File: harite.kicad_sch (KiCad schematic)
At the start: 10 parts

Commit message: Layout switches
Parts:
- removed S6: SKRHADE010, SKRHADE010, symbol SKRHADE010:SKRHADE010
- added D10, D11, D12, D13, D14, D15, D16, D17, D18, D19, D20, D21, D22, D23, D24, D25, D5, D6, D7, D8, D9: D, footprints:D_SOD123, symbol Device:D
- added U1: rp2040-zero, footprints:rp2040-zero-tht, symbol mcu:rp2040-zero
- D1, D2, D3, D4: footprint (none) -> footprints:D_SOD123
- S1, S2, S3, S4, S5: footprint SKRHADE010 -> footprints:SKRHADE010
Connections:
- net at S1.2 (CENTER): now also D5.2 (A)
- net at S1.3 (C): now also D2.2 (A)
- net at S1.4 (B): now also D4.2 (A)
- net Col 1: now reaches S1.5 (COMMON)
- net Col 1: now also U1.10 (9)
- net at S1.6 (D): now also D3.2 (A)
- net at S3.1 (A): now also D11.2 (A)
- net at S3.2 (CENTER): now also D12.2 (A)
- net at S3.3 (C): now also D13.2 (A)
- net at S3.4 (B): now also D14.2 (A)
- net Col 3: now reaches S3.5 (COMMON)
- net Col 3: now also U1.12 (11)
- net at S3.6 (D): now also D15.2 (A)
- net Row 1: now reaches D1.1 (K)
- net Row 1: now also D11.1 (K), D16.1 (K), D21.1 (K), D6.1 (K), U1.15 (14)
- net at S2.1 (A): now also D6.2 (A)
- net at S2.2 (CENTER): now also D7.2 (A)
- net at S2.3 (C): now also D8.2 (A)
- net at S2.4 (B): now also D9.2 (A)
- net Col 2: now reaches S2.5 (COMMON)
- net Col 2: now also U1.11 (10)
- net at S2.6 (D): now also D10.2 (A)
- net at S4.1 (A): now also D16.2 (A)
- net at S4.2 (CENTER): now also D17.2 (A)
- net at S4.3 (C): now also D18.2 (A)
- net at S4.4 (B): now also D19.2 (A)
- net Col 4: now reaches S4.5 (COMMON)
- net Col 4: now also U1.13 (12)
- net at S4.6 (D): now also D20.2 (A)
- net Row 5: now reaches D3.1 (K)
- net Row 5: now also D10.1 (K), D15.1 (K), D20.1 (K), D25.1 (K), U1.19 (28)
- net Row 4: now reaches D4.1 (K)
- net Row 4: now also D14.1 (K), D19.1 (K), D24.1 (K), D9.1 (K), U1.18 (27)
- net Row 2: now reaches D2.1 (K)
- net Row 2: now also D13.1 (K), D18.1 (K), D23.1 (K), D8.1 (K), U1.16 (15)
- net at S5.1 (A): now also D21.2 (A)
- net at S5.2 (CENTER): now also D22.2 (A)
- net at S5.3 (C): now also D23.2 (A)
- net at S5.4 (B): now also D24.2 (A)
- net Col 5: now reaches S5.5 (COMMON)
- net Col 5: now also U1.14 (13)
- net at S5.6 (D): now also D25.2 (A)
- new net Row 3: D12.1 (K), D17.1 (K), D22.1 (K), D5.1 (K), D7.1 (K), U1.17 (26)
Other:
- moved on the sheet: S1

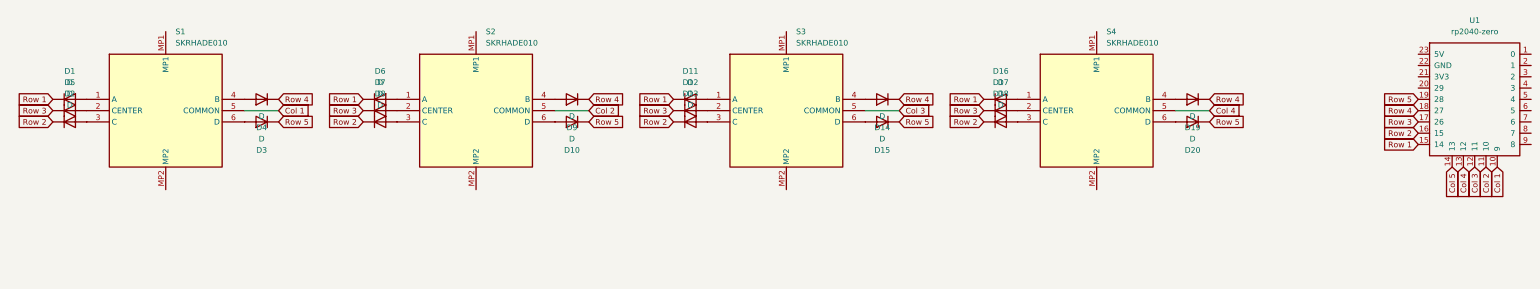
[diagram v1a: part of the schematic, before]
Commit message: Add scottokeebs
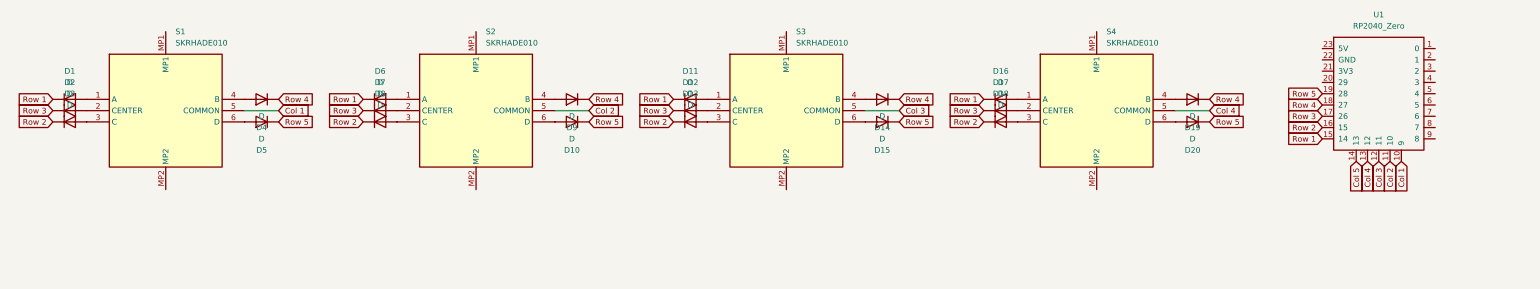
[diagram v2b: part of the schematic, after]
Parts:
- removed U1: rp2040-zero, footprints:rp2040-zero-tht, symbol mcu:rp2040-zero
- added U1: RP2040_Zero, ScottoKeebs_MCU:RP2040_Zero, symbol ScottoKeebs:MCU_RP2040_Zero
- D1, D10, D11, D12, D13, D14, D15, D16, D17, D18, D19, D20, D21, D22, D23, D24, D25, D4, D6, D7, D8, D9: footprint footprints:D_SOD123 -> ScottoKeebs_Components:Diode_SOD-123
- D2: renamed from D5; footprint footprints:D_SOD123 -> ScottoKeebs_Components:Diode_SOD-123
- D3: renamed from D2; footprint footprints:D_SOD123 -> ScottoKeebs_Components:Diode_SOD-123
- D5: renamed from D3; footprint footprints:D_SOD123 -> ScottoKeebs_Components:Diode_SOD-123
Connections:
- net Col 1: now also U1.10 (9)
- net Col 2: now also U1.11 (10)
- net Col 3: now also U1.12 (11)
- net Col 4: now also U1.13 (12)
- net Col 5: now also U1.14 (13)
- net Row 1: now also U1.15 (14)
- net Row 2: now also U1.16 (15)
- net Row 3: now also U1.17 (26)
- net Row 4: now also U1.18 (27)
- net Row 5: now also U1.19 (28)

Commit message: Add trrs
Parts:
- added U2: TRRS, ScottoKeebs_Components:TRRS_PJ-320A, symbol ScottoKeebs:Placeholder_TRRS
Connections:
- net Row 2: now also D12.1 (K), D17.1 (K), D2.1 (K), D22.1 (K), D7.1 (K); no longer D13.1 (K), D18.1 (K), D23.1 (K), D3.1 (K), D8.1 (K)
- net Row 3: now also D13.1 (K), D18.1 (K), D23.1 (K), D3.1 (K), D8.1 (K); no longer D12.1 (K), D17.1 (K), D2.1 (K), D22.1 (K), D7.1 (K)
- net GP0: now reaches U1.1 (0)
- net GP0: now also U2.4 (RING2)
- net GP1: now reaches U1.2 (1)
- net GP1: now also U2.3 (RING1)
- net 3V3: now reaches U1.21 (3V3)
- net GND: now reaches U1.22 (GND)
- net GND: now also U2.1 (SLEEVE)
- net 5V: now reaches U1.23 (5V)
- net 5V: now also U2.2 (TIP)

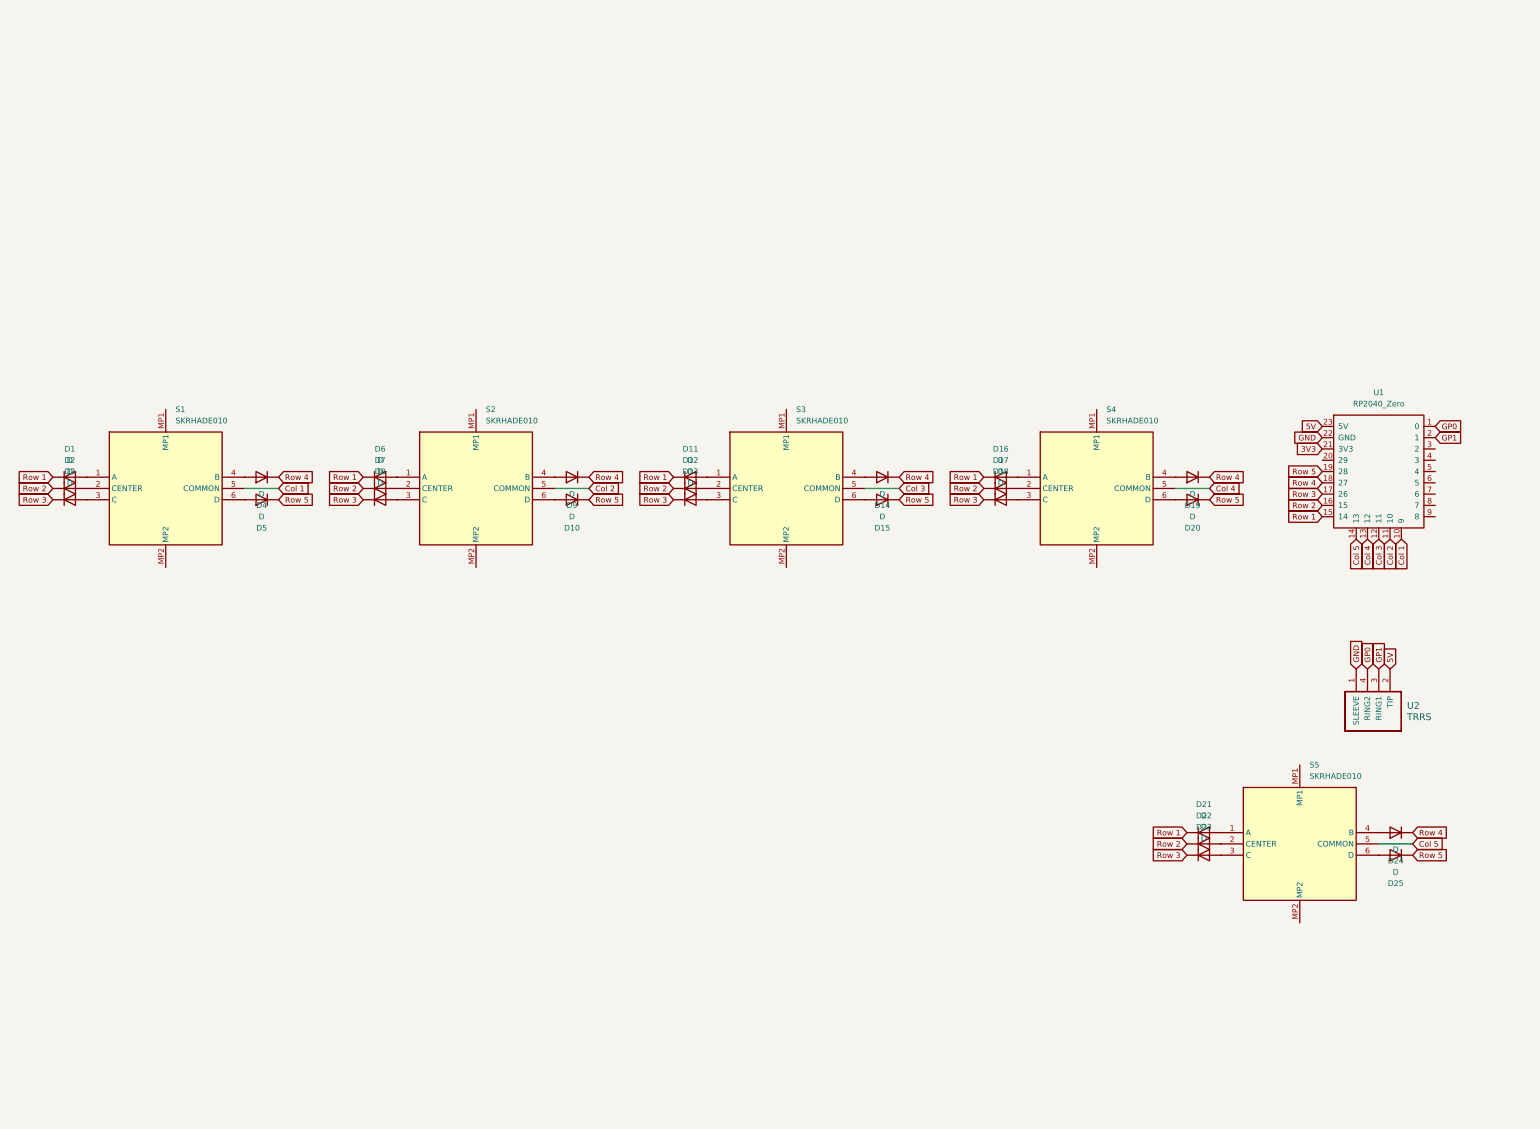
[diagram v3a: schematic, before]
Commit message: Add usbc and cirque
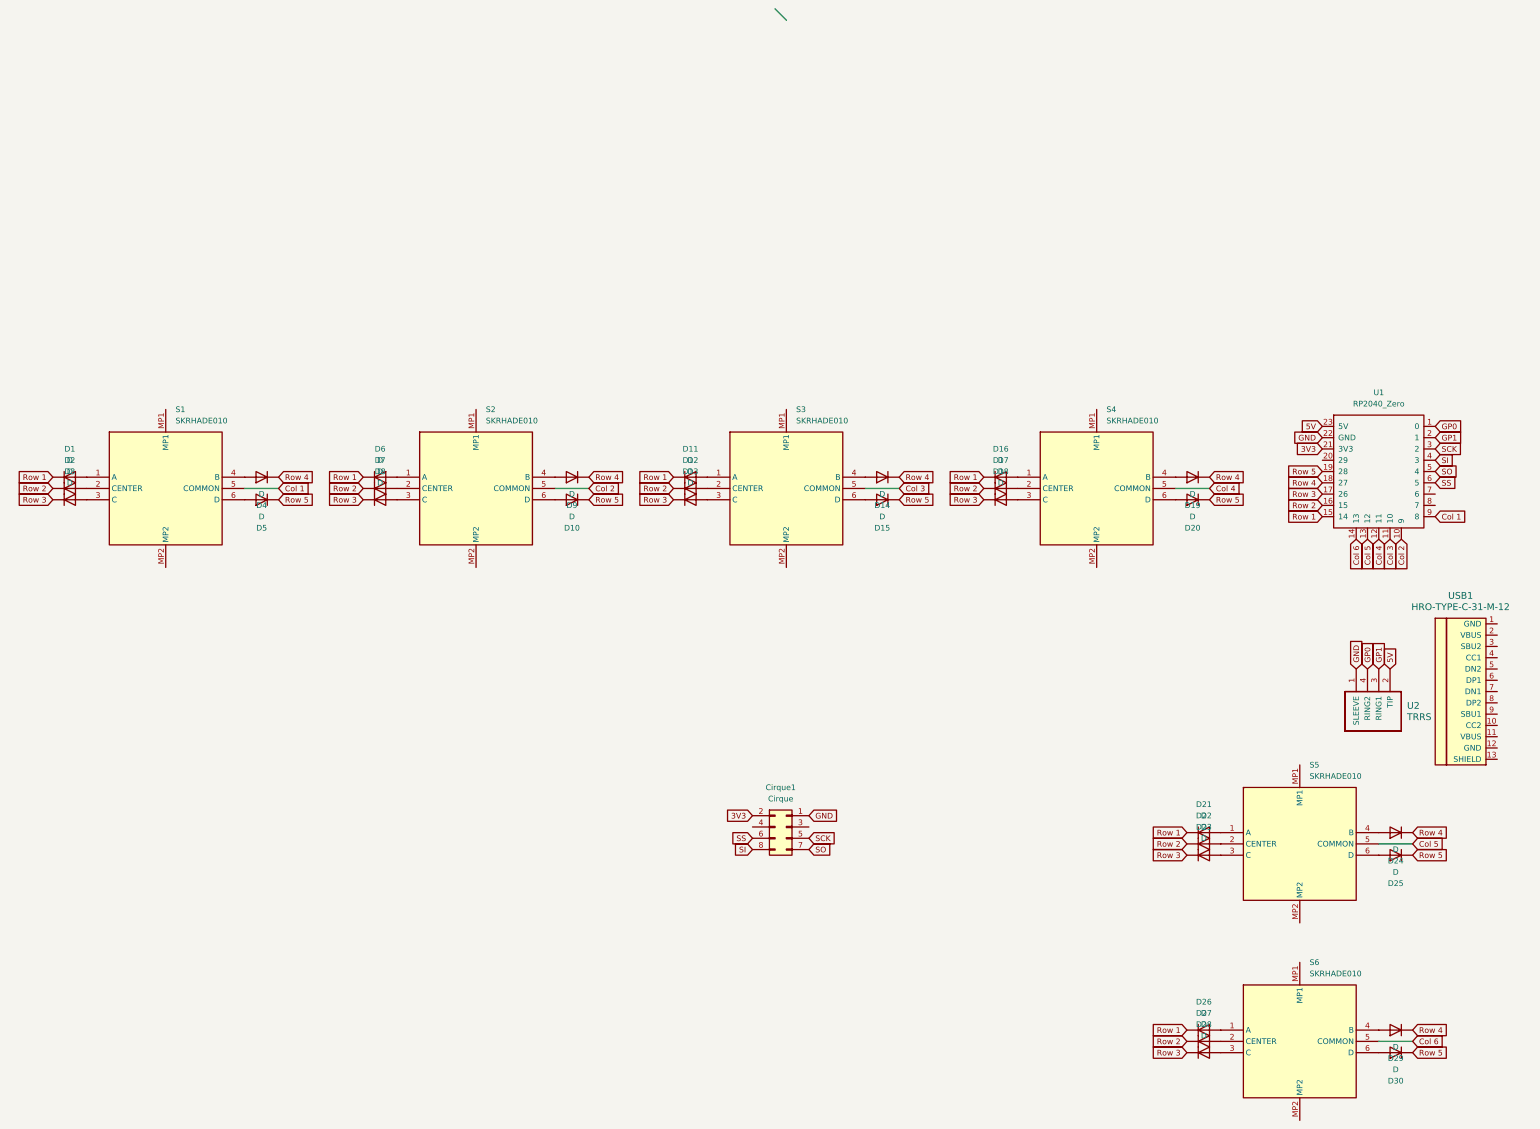
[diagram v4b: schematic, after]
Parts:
- added Cirque1: Cirque, footprints:CIRQUE-TM040040, symbol Connector_Generic:Conn_02x04_Top_Bottom
- added D26, D27, D28, D29, D30: D, ScottoKeebs_Components:Diode_SOD-123, symbol Device:D
- added S6: SKRHADE010, footprints:SKRHADE010, symbol SKRHADE010:SKRHADE010
- added USB1: HRO-TYPE-C-31-M-12, ScottoKeebs_Components:USB_C_HRO_TYPE-C-31-M-12, symbol USBType-C:HRO-TYPE-C-31-M-12
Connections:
- net 3V3: now also Cirque1.2 (Pin_2)
- net Col 1: now also U1.9 (8); no longer U1.10 (9)
- net Col 2: now also U1.10 (9); no longer U1.11 (10)
- net Col 3: now also U1.11 (10); no longer U1.12 (11)
- net Col 4: now also U1.12 (11); no longer U1.13 (12)
- net Col 5: now also U1.13 (12); no longer U1.14 (13)
- net GND: now also Cirque1.1 (Pin_1)
- net Row 1: now also D26.1 (K)
- net Row 2: now also D27.1 (K)
- net Row 3: now also D28.1 (K)
- net Row 4: now also D29.1 (K)
- net Row 5: now also D30.1 (K)
- net SCK: now reaches U1.3 (2)
- net SCK: now also Cirque1.5 (Pin_5)
- net SI: now reaches U1.4 (3)
- net SI: now also Cirque1.8 (Pin_8)
- net SO: now reaches U1.5 (4)
- net SO: now also Cirque1.7 (Pin_7)
- net SS: now reaches U1.6 (5)
- net SS: now also Cirque1.6 (Pin_6)
- new net: D27.2 (A), S6.2 (CENTER)
- new net: D26.2 (A), S6.1 (A)
- new net: D28.2 (A), S6.3 (C)
- new net: D29.2 (A), S6.4 (B)
- new net: D30.2 (A), S6.6 (D)
- new net Col 6: S6.5 (COMMON), U1.14 (13)

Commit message: update usbc
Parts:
- removed U2: TRRS, ScottoKeebs_Components:TRRS_PJ-320A, symbol ScottoKeebs:Placeholder_TRRS
- USB1: footprint ScottoKeebs_Components:USB_C_HRO_TYPE-C-31-M-12 -> footprints:HRO-TYPE-C-31-M-12
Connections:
- net 5V: now also USB1.2 (VBUS)
- net GND: now also USB1.1 (GND), USB1.12 (GND), USB1.13 (SHIELD)
- net GP0: now also USB1.5 (DN2), USB1.6 (DP1)
- net GP1: now also USB1.7 (DN1), USB1.8 (DP2)
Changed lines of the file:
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@@
 		)
 	)
-	(global_label "5V"
+	(global_label "GP0"
 		(shape input)
-		(at 321.31 99.06 90)
+		(at 345.44 101.6 0)
 		(fields_autoplaced yes)
 		(effects
@@
 		)
 		(property "Intersheetrefs" "${INTERSHEET_REFS}"
-			(at 321.31 93.7767 90)
+			(at 352.1747 101.6 0)
 			(effects
 				(font
@@
 		)
 	)
-	(global_label "GP1"
+	(global_label "Row 2"
+		(shape input)
+		(at 90.17 58.42 180)
+		(fields_autoplaced yes)
+		(effects
+			(font
+				(size 1.27 1.27)
+			)
+			(justify right)
+		)
+		(property "Intersheetrefs" "${INTERSHEET_REFS}"
+			(at 81.2582 58.42 0)
+			(effects
+				(font
+					(size 1.27 1.27)
+				)
+				(justify right)
+				(hide yes)
+			)
+		)
+	)
+	(global_label "SO"
 		(shape input)
-		(at 318.77 99.06 90)
+		(at 331.47 54.61 0)
 		(fields_autoplaced yes)
 		(effects
@@
 		)
 		(property "Intersheetrefs" "${INTERSHEET_REFS}"
-			(at 318.77 92.3253 90)
+			(at 336.9952 54.61 0)
 			(effects
 				(font
@@
 		)
 	)
-	(global_label "Row 2"
+	(global_label "Row 1"
 		(shape input)
-		(at 90.17 58.42 180)
+		(at 90.17 55.88 180)
 		(fields_autoplaced yes)
 		(effects
@@
 		)
 		(property "Intersheetrefs" "${INTERSHEET_REFS}"
-			(at 81.2582 58.42 0)
+			(at 81.2582 55.88 0)
 			(effects
 				(font
@@
 		)
 	)
-	(global_label "SO"
+	(global_label "GP1"
 		(shape input)
-		(at 331.47 54.61 0)
+		(at 345.44 104.14 0)
 		(fields_autoplaced yes)
 		(effects
@@
 		)
 		(property "Intersheetrefs" "${INTERSHEET_REFS}"
-			(at 336.9952 54.61 0)
+			(at 352.1747 104.14 0)
 			(effects
 				(font
@@
 		)
 	)
-	(global_label "Row 1"
+	(global_label "GND"
 		(shape input)
-		(at 90.17 55.88 180)
+		(at 345.44 88.9 0)
 		(fields_autoplaced yes)
 		(effects
@@
 				(size 1.27 1.27)
 			)
-			(justify right)
+			(justify left)
 		)
 		(property "Intersheetrefs" "${INTERSHEET_REFS}"
-			(at 81.2582 55.88 0)
+			(at 352.2957 88.9 0)
 			(effects
 				(font
 					(size 1.27 1.27)
 				)
-				(justify right)
+				(justify left)
 				(hide yes)
 			)
@@
 		)
 	)
+	(global_label "5V"
+		(shape input)
+		(at 345.44 91.44 0)
+		(fields_autoplaced yes)
+		(effects
+			(font
+				(size 1.27 1.27)
+			)
+			(justify left)
+		)
+		(property "Intersheetrefs" "${INTERSHEET_REFS}"
+			(at 350.7233 91.44 0)
+			(effects
+				(font
+					(size 1.27 1.27)
+				)
+				(justify left)
+				(hide yes)
+			)
+		)
+	)
+	(global_label "GND"
+		(shape input)
+		(at 345.44 116.84 0)
+		(fields_autoplaced yes)
+		(effects
+			(font
+				(size 1.27 1.27)
+			)
+			(justify left)
+		)
+		(property "Intersheetrefs" "${INTERSHEET_REFS}"
+			(at 352.2957 116.84 0)
+			(effects
+				(font
+					(size 1.27 1.27)
+				)
+				(justify left)
+				(hide yes)
+			)
+		)
+	)
 	(global_label "SCK"
 		(shape input)
@@
 		)
 	)
+	(global_label "GP0"
+		(shape input)
+		(at 345.44 99.06 0)
+		(fields_autoplaced yes)
+		(effects
+			(font
+				(size 1.27 1.27)
+			)
+			(justify left)
+		)
+		(property "Intersheetrefs" "${INTERSHEET_REFS}"
+			(at 352.1747 99.06 0)
+			(effects
+				(font
+					(size 1.27 1.27)
+				)
+				(justify left)
+				(hide yes)
+			)
+		)
+	)
 	(global_label "Row 2"
 		(shape input)
@@
 		)
 	)
+	(global_label "GND"
+		(shape input)
+		(at 345.44 119.38 0)
+		(fields_autoplaced yes)
+		(effects
+			(font
+				(size 1.27 1.27)
+			)
+			(justify left)
+		)
+		(property "Intersheetrefs" "${INTERSHEET_REFS}"
+			(at 352.2957 119.38 0)
+			(effects
+				(font
+					(size 1.27 1.27)
+				)
+				(justify left)
+				(hide yes)
+			)
+		)
+	)
 	(global_label "Col 1"
 		(shape input)
@@
 		)
 	)
+	(global_label "GP1"
+		(shape input)
+		(at 345.44 106.68 0)
+		(fields_autoplaced yes)
+		(effects
+			(font
+				(size 1.27 1.27)
+			)
+			(justify left)
+		)
+		(property "Intersheetrefs" "${INTERSHEET_REFS}"
+			(at 352.1747 106.68 0)
+			(effects
+				(font
+					(size 1.27 1.27)
+				)
+				(justify left)
+				(hide yes)
+			)
+		)
+	)
 	(global_label "Row 3"
 		(shape input)
@@
 		)
 	)
-	(global_label "GND"
-		(shape input)
-		(at 313.69 99.06 90)
-		(fields_autoplaced yes)
-		(effects
-			(font
-				(size 1.27 1.27)
-			)
-			(justify left)
-		)
-		(property "Intersheetrefs" "${INTERSHEET_REFS}"
-			(at 313.69 92.2043 90)
-			(effects
-				(font
-					(size 1.27 1.27)
-				)
-				(justify left)
-				(hide yes)
-			)
-		)
-	)
 	(global_label "3V3"
 		(shape input)
@@
 		)
 	)
-	(global_label "GP0"
-		(shape input)
-		(at 316.23 99.06 90)
-		(fields_autoplaced yes)
-		(effects
-			(font
-				(size 1.27 1.27)
-			)
-			(justify left)
-		)
-		(property "Intersheetrefs" "${INTERSHEET_REFS}"
-			(at 316.23 92.3253 90)
-			(effects
-				(font
-					(size 1.27 1.27)
-				)
-				(justify left)
-				(hide yes)
-			)
-		)
-	)
 	(symbol
 		(lib_id "Device:D")
@@
 			)
 		)
-		(property "Footprint" "ScottoKeebs_Components:USB_C_HRO_TYPE-C-31-M-12"
+		(property "Footprint" "footprints:HRO-TYPE-C-31-M-12"
 			(at 342.9 102.87 0)
 			(effects
@@
 					(unit 1)
 				)
-			)
-		)
-	)
-	(symbol
-		(lib_id "ScottoKeebs:Placeholder_TRRS")
-		(at 311.15 107.95 270)
-		(unit 1)
-		(exclude_from_sim no)
-		(in_bom yes)
-		(on_board yes)
-		(dnp no)
-		(fields_autoplaced yes)
-		(property "Reference" "U2"
-			(at 325.12 107.3149 90)
-			(effects
-				(font
-					(size 1.524 1.524)
-				)
-				(justify left)
-			)
-		)
-		(property "Value" "TRRS"
-			(at 325.12 109.8549 90)
-			(effects
-				(font
-					(size 1.524 1.524)
-				)
-				(justify left)
-			)
-		)
-		(property "Footprint" "ScottoKeebs_Components:TRRS_PJ-320A"
-			(at 311.15 111.76 0)
-			(effects
-				(font
-					(size 1.524 1.524)
-				)
-				(hide yes)
-			)
-		)
-		(property "Datasheet" ""
-			(at 311.15 111.76 0)
-			(effects
-				(font
-					(size 1.524 1.524)
-				)
-				(hide yes)
-			)
-		)
-		(property "Description" ""
-			(at 311.15 107.95 0)
-			(effects
-				(font
-					(size 1.27 1.27)
-				)
-				(hide yes)
-			)
-		)
-		(pin "2"
-		)
-		(pin "3"
-		)
-		(pin "1"
-		)
-		(pin "4"
-		)
-		(instances
-			(project "harite"
-				(path "/feb70c3f-3e34-4f8f-9694-07d231f2d237"
-					(reference "U2")
-					(unit 1)
-				)
